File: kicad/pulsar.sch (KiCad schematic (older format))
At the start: 6 parts

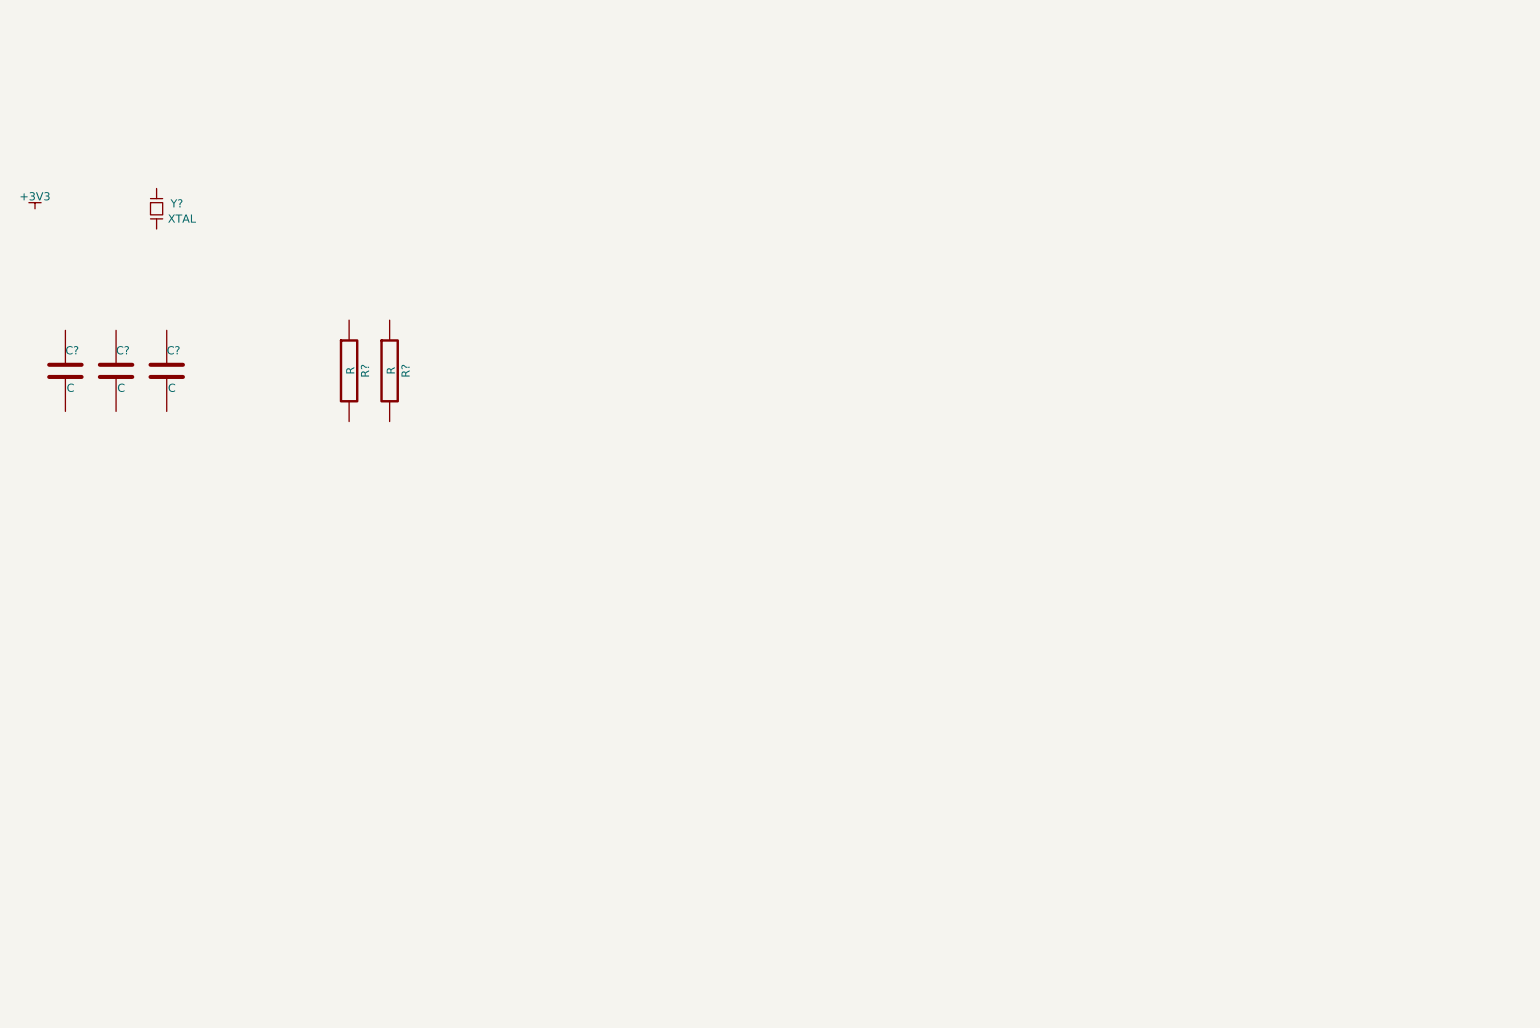
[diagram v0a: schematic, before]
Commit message: update nrf51 lib, basic nrf schematic
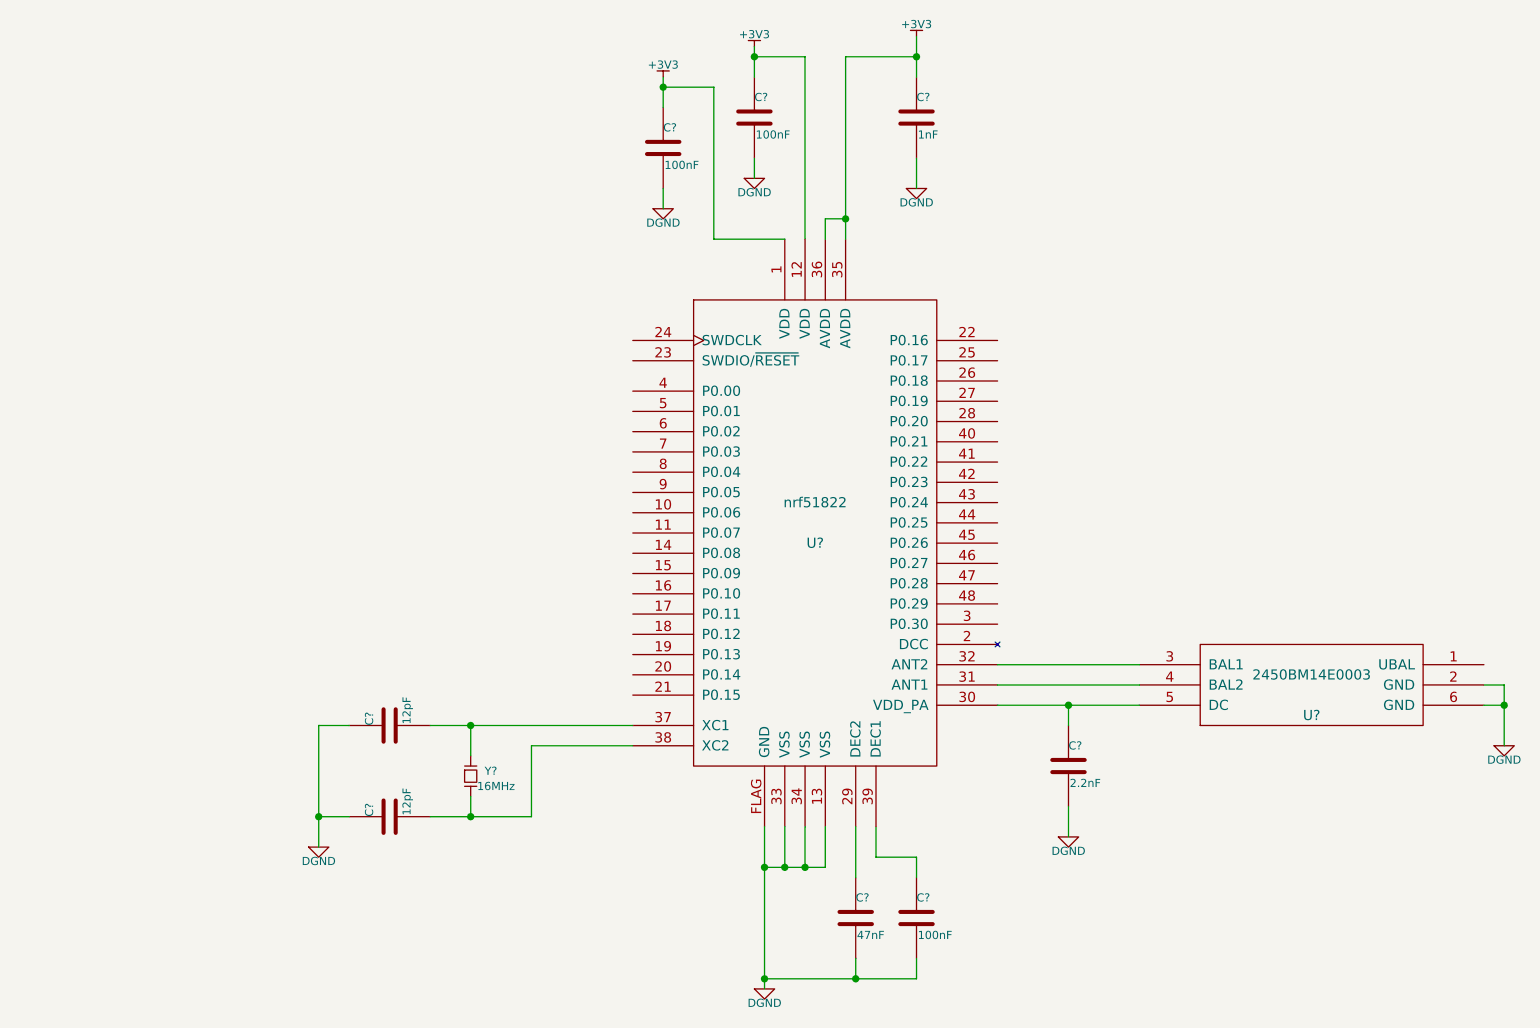
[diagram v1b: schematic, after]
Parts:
- removed C? (x3): C, symbol C
- removed R? (x2): R, symbol R
- removed Y?: XTAL, symbol XTAL
- added C?: 47nF, symbol C
- added C? (x3): 100nF, symbol C
- added C? (x2): 12pF, symbol C
- added C?: 2.2nF, symbol C
- added C?: 1nF, symbol C
- added U?: nrf51822, MODULE, symbol nrf51822
- added U?: 2450BM14E0003, MODULE, symbol 2450BM14E0003
- added Y?: 16MHz, symbol XTAL
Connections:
- net +3V3: now also C?.1, C?.1, C?.1, U?.1 (VDD), U?.12 (VDD), U?.35 (AVDD), U?.36 (AVDD)
- new net: C?.1, U?.29 (DEC2)
- new net: C?.1, U?.30 (VDD_PA), U?.5 (DC)
- new net: U?.31 (ANT1), U?.4 (BAL2)
- new net: U?.3 (BAL1), U?.32 (ANT2)
- new net: C?.2, U?.37 (XC1), Y?.2
- new net: C?.2, U?.38 (XC2), Y?.1
- new net: C?.1, U?.39 (DEC1)
- new net DGND: C?.1, C?.1, C?.2, C?.2, C?.2, C?.2, C?.2, C?.2, U?.13 (VSS), U?.2 (GND), U?.33 (VSS), U?.34 (VSS), U?.6 (GND), U?.FLAG (GND)

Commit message: symbol rework
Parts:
- removed U?: 2450BM14E0003, MODULE, symbol 2450BM14E0003
- added B?: nRF-BALUN, 2450BM14E0003, symbol nRF-BALUN
- added U?: nrf51822, MODULE, symbol nrf51822
- added U?: XO2-256, MODULE, symbol XO2-256
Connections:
- net labels added: ANT
- wire segments 44 -> 48
- no-connect marks 0 -> 1
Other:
- moved on the sheet: C?, U?, Y?

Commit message: update schematic
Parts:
- added AE?: ANT, symbol ANT
- added C?: 1u, symbol C
- added C?: 2.2u, symbol C
- added C? (x10): C, symbol C
- added C?: 47n, symbol C
- added FB?: FERRITE, symbol FERRITE
- added J?: POWER, symbol CONN-2
- added R?: 190k, symbol R
- added R?: 10k, symbol R
- added R?: 5m, symbol R
- added S?: TACTILE-4, symbol TACTILE-4
- added U?: MIC5205, symbol MIC5205
- added U?: TS1102, symbol TS1102
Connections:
- net labels added: CH1, CH10, CH11, CH12, CH2, CH3, CH4, CH5, CH6, CH7, CH8, CH9, IIN_SENSE, NRF_SWDCLK, NRF_SWDIO/~RESET, PAIR_BUTTON, PGND, SPI_CLK, SPI_CS, SPI_MISO, SPI_MOSI, VIN, VIN_SENSE, XO2_JTAG_TCK, XO2_JTAG_TDI, XO2_JTAG_TDO, XO2_JTAG_TMS, ~XO2_JTAG_EN, ~XO2_RESET
- wire segments 48 -> 167
- no-connect marks 1 -> 3
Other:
- note added: "VIN max: 16V\nsense max: 1.2V"
- note added: "XXX temp sensor for ground plane?\nNTC chip thermistor voltage divider"
- moved on the sheet: U?

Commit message: add temp sense, rearrange schematic
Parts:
- removed C?: 47n, symbol C
- added C? (x3): 47n, symbol C
- added R?: 22k, symbol R
- added RT?: 47k, symbol NTC
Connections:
- net labels added: TEMP_SENSE
- wire segments 167 -> 212
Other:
- note added: "XXX or star ground?"
- note added: "missing:\n- JTAG header\n- SWD header\n- aux connector header"
- note added: "place NTC on heat sink GND pour"
- note removed: "XXX temp sensor for ground plane?\nNTC chip thermistor voltage divider"
- moved on the sheet: C?, R?, U?, Y?

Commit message: add headers
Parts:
- added D? (x3): LED, symbol LED
- added J?: JTAG, symbol JTAG
- added J?: XO2-JTAG, symbol JTAG
- added J?: CONN-2x5, symbol CONN-2x5
- added R? (x3): 1k, symbol R
- added S?: TACTILE-4, symbol TACTILE-4
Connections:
- net labels added: AUX1, AUX2, AUX3, AUX4, AUX5, BUTTON1, BUTTON2, LED1, LED2, LED3
- net labels removed: PAIR_BUTTON
- wire segments 212 -> 218
- no-connect marks 3 -> 8
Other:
- note removed: "missing:\n- JTAG header\n- SWD header\n- aux connector header"
- moved on the sheet: C?, U?, Y?

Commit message: add uart to swd connector
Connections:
- net labels added: RX, TX
- wire segments 218 -> 222
- no-connect marks 8 -> 6
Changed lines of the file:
@@
 Text Label 7350 2200 0    50   ~ 0
 NRF_SWDIO/~RESET
-$Comp
-L DGND #PWR?
-U 1 1 542F56C5
-P 8550 -250
-F 0 "#PWR?" V 8670 -250 60  0001 C CNN
-F 1 "DGND" H 8550 -350 40  0000 C CNN
-F 2 "" H 8550 -300 60  0000 C CNN
-F 3 "" H 8550 -300 60  0000 C CNN
-	1    8550 -250
-	-1   0    0    -1
-$EndComp
 NoConn ~ 4750 4250
 Text Label 5400 4150 2    50   ~ 0
@@
 NoConn ~ 8800 4450
 NoConn ~ 10000 4450
-NoConn ~ 10000 4350
-NoConn ~ 10000 4250
 Text Label 10850 4150 2    50   ~ 0
 NRF_SWDCLK
@@
 Text Label 8700 6200 0    50   ~ 0
 AUX5
+Wire Wire Line
+	6050 2250 6600 2250
+Text Label 6600 2350 2    50   ~ 0
+RX
+Wire Wire Line
+	6600 2350 6050 2350
+Text Label 6600 2250 2    50   ~ 0
+TX
+Wire Wire Line
+	10000 4250 10550 4250
+Text Label 10550 4350 2    50   ~ 0
+RX
+Wire Wire Line
+	10550 4350 10000 4350
+Text Label 10550 4250 2    50   ~ 0
+TX
 $EndSCHEMATC

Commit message: add 32kHz crystal
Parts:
- added C? (x2): 12pF, symbol C
- added Y?: 32kHz, symbol XTAL
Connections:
- wire segments 222 -> 231
- no-connect marks 6 -> 10
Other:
- moved on the sheet: C?, U?

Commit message: start assigning footprints
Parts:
- B1: renamed from B?; footprint 2450BM14E0003 -> (none)
- C1, C10, C11, C12, C13, C14, C15, C16, C17, C18, C19, C2, C20, C21, C22, C23, C24, C25, C3, C4, C5, C7, C8, C9: renamed from C?; footprint (none) -> SMD-1005:SMD-1005
- C6: renamed from C?; footprint (none) -> SMD-1608:SMD-1608
- D1, D2, D3: renamed from D?; footprint (none) -> SMD-1005:SMD-1005
- FB1: renamed from FB?; footprint (none) -> SMD-1005:SMD-1005
- R1, R2, R4, R5, R6, R7: renamed from R?; footprint (none) -> SMD-1608:SMD-1608
- R3: renamed from R?; footprint (none) -> SMD-2012:SMD-2012
- RT1: renamed from RT?; footprint (none) -> SMD-1608:SMD-1608
- U1, U3: renamed from U?; footprint (none) -> sot-23-5:SOT-23-5
- U2: renamed from U?; footprint MODULE -> pulsar:xo2-256-qfn32
- U4: renamed from U?; footprint MODULE -> pulsar:nrf51822-qfn48
- Y2: renamed from Y?; footprint (none) -> osc2520:OSC2520
- gave numbers to parts that had none: 8
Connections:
- net labels added: POWER_FLAG
- wire segments 231 -> 232
